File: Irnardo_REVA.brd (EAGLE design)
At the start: 12 x 17 mm, 20 parts, among them J1 USB_PAD, U1 ATMEGA32U4-MU, U2 TSOP755, X1 16MHz

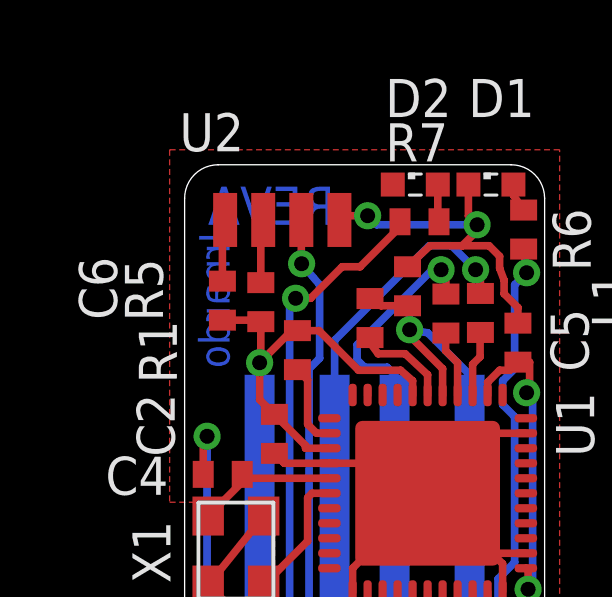
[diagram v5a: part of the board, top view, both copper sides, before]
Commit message: Fix de-couple cap on IR receiver
C6 de-coupling U2 was wrong side of R5.
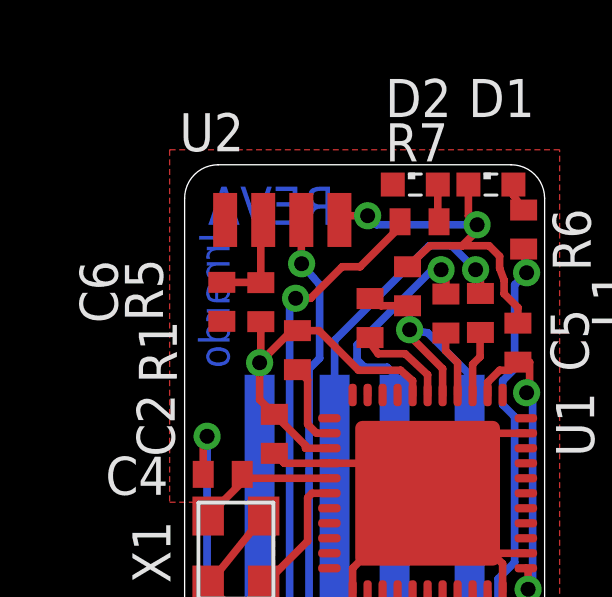
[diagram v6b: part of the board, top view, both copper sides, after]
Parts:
- turned C6 to 270 degrees
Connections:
- net +5V: no longer C6.1
- net N$5: now also C6.1
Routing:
- net GND: track 49.5 -> 47.6 mm
- net N$5: track 2.12 -> 3.43 mm
- net +5V: track 47.7 -> 46.5 mm
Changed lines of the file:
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@@
 <?xml version="1.0" encoding="utf-8"?>
 <!DOCTYPE eagle SYSTEM "eagle.dtd">
-<eagle version="6.4">
+<eagle version="6.5.0">
 <drawing>
 <settings>
@@
 <layers>
 <layer number="1" name="Top" color="4" fill="1" visible="yes" active="yes"/>
-<layer number="16" name="Bottom" color="1" fill="1" visible="no" active="yes"/>
+<layer number="16" name="Bottom" color="1" fill="1" visible="yes" active="yes"/>
 <layer number="17" name="Pads" color="2" fill="1" visible="yes" active="yes"/>
 <layer number="18" name="Vias" color="2" fill="1" visible="yes" active="yes"/>
-<layer number="19" name="Unrouted" color="6" fill="1" visible="no" active="yes"/>
-<layer number="20" name="Dimension" color="15" fill="1" visible="no" active="yes"/>
-<layer number="21" name="tPlace" color="7" fill="1" visible="no" active="yes"/>
-<layer number="22" name="bPlace" color="7" fill="1" visible="no" active="yes"/>
-<layer number="23" name="tOrigins" color="15" fill="1" visible="no" active="yes"/>
-<layer number="24" name="bOrigins" color="15" fill="1" visible="no" active="yes"/>
-<layer number="25" name="tNames" color="7" fill="1" visible="no" active="yes"/>
+<layer number="19" name="Unrouted" color="6" fill="1" visible="yes" active="yes"/>
+<layer number="20" name="Dimension" color="15" fill="1" visible="yes" active="yes"/>
+<layer number="21" name="tPlace" color="7" fill="1" visible="yes" active="yes"/>
+<layer number="22" name="bPlace" color="7" fill="1" visible="yes" active="yes"/>
+<layer number="23" name="tOrigins" color="15" fill="1" visible="yes" active="yes"/>
+<layer number="24" name="bOrigins" color="15" fill="1" visible="yes" active="yes"/>
+<layer number="25" name="tNames" color="7" fill="1" visible="yes" active="yes"/>
 <layer number="26" name="bNames" color="7" fill="1" visible="no" active="yes"/>
 <layer number="27" name="tValues" color="7" fill="1" visible="no" active="yes"/>
@@
 <layer number="37" name="tTest" color="7" fill="1" visible="no" active="yes"/>
 <layer number="38" name="bTest" color="7" fill="1" visible="no" active="yes"/>
-<layer number="39" name="tKeepout" color="4" fill="11" visible="no" active="yes"/>
-<layer number="40" name="bKeepout" color="1" fill="11" visible="no" active="yes"/>
+<layer number="39" name="tKeepout" color="4" fill="11" visible="yes" active="yes"/>
+<layer number="40" name="bKeepout" color="1" fill="11" visible="yes" active="yes"/>
 <layer number="41" name="tRestrict" color="4" fill="10" visible="no" active="yes"/>
 <layer number="42" name="bRestrict" color="1" fill="10" visible="no" active="yes"/>
@@
 <attribute name="NAME" x="-0.17" y="17.45" size="1.27" layer="21"/>
 </element>
-<element name="C6" library="resistor" package="C0402" value="100n" x="1.26" y="12.47" smashed="yes" rot="R90">
-<attribute name="NAME" x="-2.252" y="11.835" size="1.27" layer="25" rot="R90"/>
-<attribute name="VALUE" x="3.165" y="11.835" size="1.27" layer="27" rot="R90"/>
+<element name="C6" library="resistor" package="C0402" value="100n" x="1.24" y="12.43" smashed="yes" rot="R270">
+<attribute name="NAME" x="-3.498" y="13.815" size="1.27" layer="25" rot="R270"/>
+<attribute name="VALUE" x="-0.665" y="13.065" size="1.27" layer="27" rot="R270"/>
 </element>
 <element name="R5" library="resistor" package="R0402" value="100R" x="2.54" y="12.42" smashed="yes" rot="R90">
@@
 <contactref element="C7" pad="1"/>
 <contactref element="R5" pad="1"/>
-<contactref element="C6" pad="1"/>
 <contactref element="J1" pad="V+"/>
 <wire x1="11.11" y1="10.42" x2="10.84" y2="10.15" width="0.254" layer="1"/>
@@
 <wire x1="2.54" y1="11.77" x2="2.54" y2="10.44" width="0.254" layer="1"/>
 <wire x1="2.54" y1="10.44" x2="2.5" y2="10.4" width="0.254" layer="1"/>
-<wire x1="1.26" y1="11.82" x2="2.49" y2="11.82" width="0.254" layer="1"/>
 <wire x1="2.49" y1="11.82" x2="2.54" y2="11.77" width="0.254" layer="1"/>
 <wire x1="4.03" y1="7.55" x2="4.03" y2="7.64" width="0.254" layer="1"/>
@@
 <contactref element="C4" pad="2"/>
 <contactref element="L1" pad="2"/>
-<contactref element="C6" pad="2"/>
 <contactref element="U2" pad="1"/>
 <contactref element="U2" pad="4"/>
@@
 <wire x1="5.6" y1="3.55" x2="8.1" y2="6.05" width="0.254" layer="1"/>
 <wire x1="2.635" y1="5.29" x2="0.785" y2="2.99" width="0.254" layer="1"/>
-<wire x1="1.26" y1="13.12" x2="1.26" y2="15.07" width="0.254" layer="1"/>
 <wire x1="1.26" y1="15.07" x2="1.35" y2="15.16" width="0.254" layer="1"/>
 <wire x1="9.46" y1="16.34" x2="9.46" y2="15.29" width="0.254" layer="1"/>
@@
 <wire x1="9.25" y1="14.3" x2="9.75" y2="14.8" width="0.254" layer="1"/>
 <wire x1="9.75" y1="14.8" x2="9.75" y2="15" width="0.254" layer="1"/>
+<contactref element="C6" pad="2"/>
 </signal>
 <signal name="RESET">
@@
 <wire x1="2.54" y1="13.07" x2="2.54" y2="15.08" width="0.254" layer="1"/>
 <wire x1="2.54" y1="15.08" x2="2.62" y2="15.16" width="0.254" layer="1"/>
+<contactref element="C6" pad="1"/>
+<wire x1="1.24" y1="13.08" x2="2.54" y2="13.08" width="0.254" layer="1"/>
+<wire x1="2.54" y1="13.08" x2="2.54" y2="13.07" width="0.254" layer="1"/>
 </signal>
 <signal name="IO13">

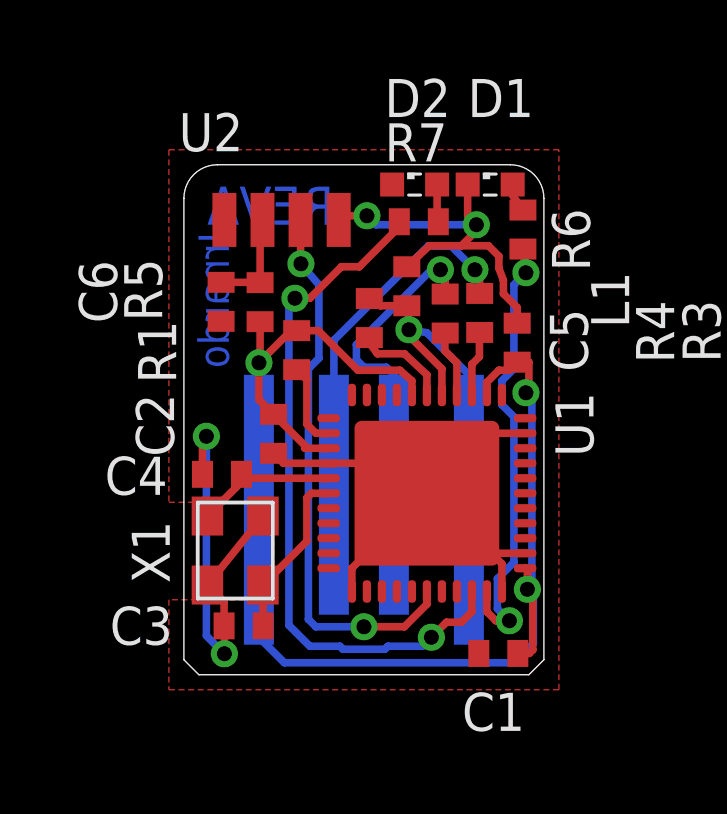
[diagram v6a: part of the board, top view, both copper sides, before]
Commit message: Swap XTAL for 2.5x2mm model
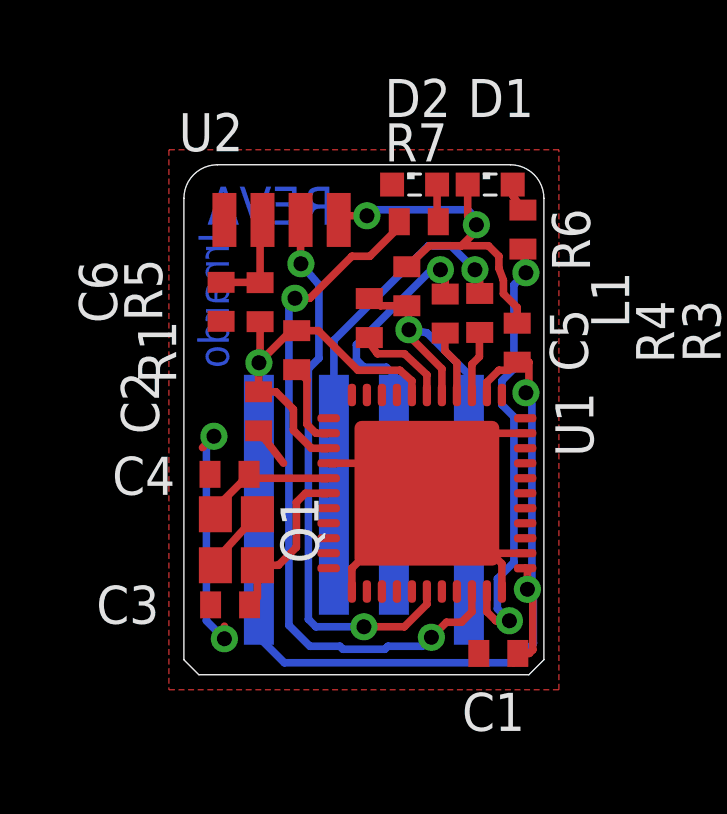
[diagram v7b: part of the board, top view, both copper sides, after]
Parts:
- removed X1: 16MHz, Arduino_Leonardo-REV3b:SMARTPRJ_CRYSTAL-3.2-2.5
- added Q1: FA-20H, crystal:FA-20H
- moved C2 0.90 mm to (2.49, 8.78)
- moved C3 0.83 mm to (1.54, 2.33)
- moved C4 0.25 mm to (1.52, 6.68)
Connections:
- net GND: now also Q1.2, Q1.4; no longer X1.2, X1.4
- net N$1: now also C4.1, Q1.1, U1.16; no longer C3.1, U1.17, X1.1
- net N$2: now also C3.1, Q1.3, U1.17; no longer C4.1, U1.16, X1.3
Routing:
- net GND: track 47.6 -> 43.0 mm
- net N$2: track 4.82 -> 5.94 mm
- net N$1: track 5.67 -> 4.93 mm

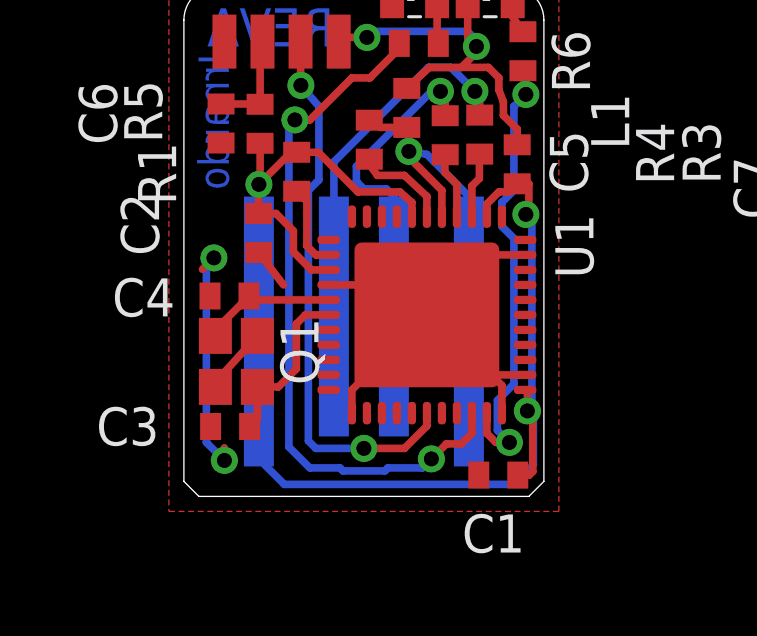
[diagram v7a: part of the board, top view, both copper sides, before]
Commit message: Finish tweaks after move to 2.5mm XTAL
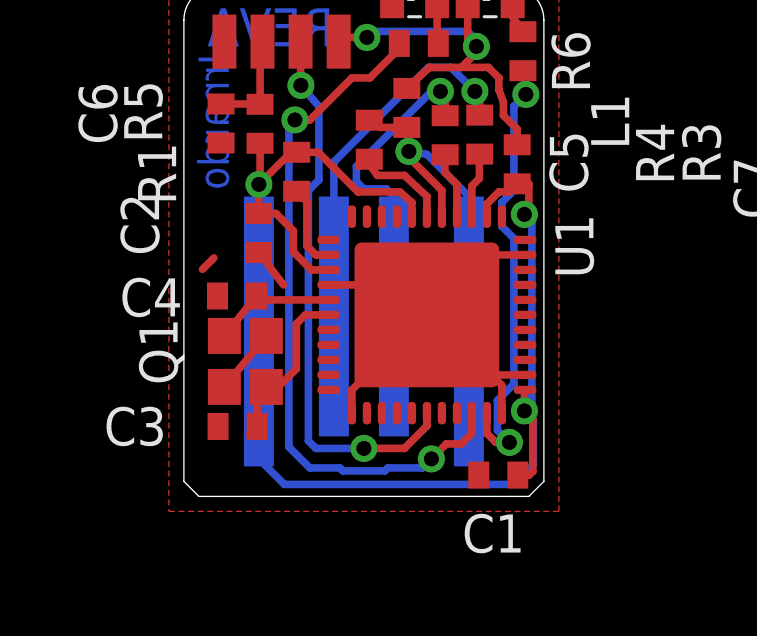
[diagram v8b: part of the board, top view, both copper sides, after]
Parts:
- moved Q1 0.30 mm to (2.05, 4.50)
- moved C3 0.25 mm to (1.79, 2.33)
- moved C4 0.25 mm to (1.77, 6.68)
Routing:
- net GND: track 43.0 -> 35.2 mm, vias 4 -> 2
- net N$1: track 4.93 -> 4.24 mm
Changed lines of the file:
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@@
 <?xml version="1.0" encoding="utf-8"?>
 <!DOCTYPE eagle SYSTEM "eagle.dtd">
-<eagle version="6.5.0">
+<eagle version="6.4">
 <drawing>
 <settings>
@@
 <attribute name="VALUE" x="11.115" y="2.615" size="1.27" layer="27" rot="R180"/>
 </element>
-<element name="C3" library="resistor" package="C0402" value="22p" x="1.54" y="2.33" smashed="yes" rot="R180">
-<attribute name="NAME" x="-0.825" y="2.968" size="1.27" layer="25" rot="R180"/>
-<attribute name="VALUE" x="2.175" y="4.235" size="1.27" layer="27" rot="R180"/>
-</element>
-<element name="C4" library="resistor" package="C0402" value="22p" x="1.52" y="6.68" smashed="yes" rot="R180">
-<attribute name="NAME" x="-0.295" y="7.268" size="1.27" layer="25" rot="R180"/>
-<attribute name="VALUE" x="2.155" y="8.585" size="1.27" layer="27" rot="R180"/>
+<element name="C3" library="resistor" package="C0402" value="22p" x="1.79" y="2.33" smashed="yes" rot="R180">
+<attribute name="NAME" x="-0.575" y="2.968" size="1.27" layer="25" rot="R180"/>
+<attribute name="VALUE" x="2.425" y="4.235" size="1.27" layer="27" rot="R180"/>
+</element>
+<element name="C4" library="resistor" package="C0402" value="22p" x="1.77" y="6.68" smashed="yes" rot="R180">
+<attribute name="NAME" x="-0.045" y="7.268" size="1.27" layer="25" rot="R180"/>
+<attribute name="VALUE" x="2.405" y="8.585" size="1.27" layer="27" rot="R180"/>
 </element>
 <element name="C2" library="resistor" package="C0402" value="100n" x="2.49" y="8.78" smashed="yes" rot="R270">
@@
 <attribute name="NAME" x="6.75" y="-1.75" size="1.27" layer="26" rot="MR0"/>
 </element>
-<element name="Q1" library="crystal" package="FA-20H" value="FA-20H" x="1.75" y="4.5" rot="R270"/>
+<element name="Q1" library="crystal" package="FA-20H" value="FA-20H" x="2.05" y="4.5" smashed="yes" rot="R270">
+<attribute name="NAME" x="-1.48" y="5.945" size="1.27" layer="25" rot="R270"/>
+<attribute name="VALUE" x="-0.7" y="5.95" size="1.27" layer="27" rot="R270"/>
+</element>
 </elements>
 <signals>
@@
 <wire x1="2.5" y1="10.4" x2="2.5" y2="10.5" width="0.254" layer="16"/>
 <wire x1="2.5" y1="10.4" x2="2.5" y2="5.5" width="0.254" layer="16"/>
-<wire x1="11.38" y1="3.545" x2="11.375" y2="3.55" width="0.254" layer="1"/>
 <wire x1="3.76" y1="11.47" x2="3.57" y2="11.47" width="0.254" layer="1"/>
 <wire x1="3.57" y1="11.47" x2="2.5" y2="10.4" width="0.254" layer="1"/>
@@
 <wire x1="11.13" y1="0.71" x2="11.51" y2="0.71" width="0.254" layer="1"/>
 <wire x1="11.51" y1="0.71" x2="11.63" y2="0.83" width="0.254" layer="1"/>
-<wire x1="11.63" y1="0.83" x2="11.63" y2="2.67" width="0.254" layer="1"/>
-<wire x1="11.63" y1="2.67" x2="11.45" y2="2.85" width="0.254" layer="1"/>
-<via x="11.45" y="2.85" extent="1-16" drill="0.5"/>
-<wire x1="11.45" y1="2.85" x2="11.6" y2="3" width="0.254" layer="16"/>
-<wire x1="11.6" y1="3" x2="11.6" y2="9.2" width="0.254" layer="16"/>
-<wire x1="11.6" y1="9.2" x2="11.4" y2="9.4" width="0.254" layer="16"/>
-<via x="11.4" y="9.4" extent="1-16" drill="0.5"/>
-<wire x1="11.4" y1="9.4" x2="11.5" y2="9.5" width="0.254" layer="1"/>
-<wire x1="11.5" y1="9.5" x2="11.5" y2="10.42" width="0.254" layer="1"/>
+<wire x1="11.63" y1="0.83" x2="11.63" y2="2.57" width="0.254" layer="1"/>
+<wire x1="11.63" y1="2.57" x2="11.35" y2="2.85" width="0.254" layer="1"/>
+<via x="11.35" y="2.85" extent="1-16" drill="0.5"/>
+<wire x1="11.35" y1="2.85" x2="11.6" y2="3.1" width="0.254" layer="16"/>
+<wire x1="11.6" y1="3.1" x2="11.6" y2="9.15" width="0.254" layer="16"/>
+<wire x1="11.6" y1="9.15" x2="11.35" y2="9.4" width="0.254" layer="16"/>
+<via x="11.35" y="9.4" extent="1-16" drill="0.5"/>
+<wire x1="11.35" y1="9.4" x2="11.5" y2="9.55" width="0.254" layer="1"/>
+<wire x1="11.5" y1="9.55" x2="11.5" y2="10.42" width="0.254" layer="1"/>
 <wire x1="11.5" y1="10.42" x2="11.11" y2="10.42" width="0.254" layer="1"/>
-<wire x1="11.375" y1="3.55" x2="11.45" y2="3.475" width="0.254" layer="1" curve="-90"/>
-<wire x1="11.45" y1="3.475" x2="11.45" y2="2.85" width="0.254" layer="1"/>
 <wire x1="2.5" y1="5.5" x2="2.5" y2="1.25" width="0.254" layer="16"/>
 <wire x1="2.5" y1="1.25" x2="3.35" y2="0.4" width="0.254" layer="16"/>
 <wire x1="3.35" y1="0.4" x2="11" y2="0.4" width="0.254" layer="16"/>
 <wire x1="11" y1="0.4" x2="11.65" y2="1.05" width="0.254" layer="16"/>
-<wire x1="11.65" y1="1.05" x2="11.65" y2="2.6" width="0.254" layer="16"/>
-<wire x1="11.65" y1="2.6" x2="11.5" y2="2.75" width="0.254" layer="16"/>
+<wire x1="11.65" y1="1.05" x2="11.65" y2="2.55" width="0.254" layer="16"/>
 <wire x1="7.6" y1="9.325" x2="7.6" y2="9.8" width="0.254" layer="1"/>
 <wire x1="7.6" y1="9.8" x2="7.2" y2="10.15" width="0.254" layer="1"/>
@@
 <wire x1="3.65" y1="8.85" x2="3.07" y2="9.43" width="0.254" layer="1"/>
 <wire x1="3.07" y1="9.43" x2="2.49" y2="9.43" width="0.254" layer="1"/>
-<wire x1="11.65" y1="2.6" x2="11.63" y2="2.67" width="0" layer="19" extent="1-16"/>
+<wire x1="11.65" y1="2.55" x2="11.35" y2="2.85" width="0.254" layer="16"/>
+<wire x1="11.375" y1="3.55" x2="11.35" y2="3.525" width="0.254" layer="1"/>
+<wire x1="11.35" y1="3.525" x2="11.35" y2="2.85" width="0.254" layer="1"/>
 </signal>
 <signal name="GND">
@@
 <wire x1="5.3" y1="15.3" x2="5.16" y2="15.16" width="0.254" layer="1"/>
 <wire x1="0.62" y1="7.57" x2="1" y2="7.95" width="0.254" layer="1"/>
-<via x="1" y="7.95" extent="1-16" drill="0.5"/>
-<wire x1="0.75" y1="1.8" x2="1.35" y2="1.2" width="0.254" layer="16"/>
-<via x="1.35" y="1.2" extent="1-16" drill="0.5"/>
-<wire x1="1.35" y1="1.2" x2="1.35" y2="1.62" width="0.254" layer="1"/>
 <wire x1="7.43" y1="13.6" x2="8.18" y2="14.3" width="0.254" layer="1"/>
 <wire x1="8.18" y1="14.3" x2="9.25" y2="14.3" width="0.254" layer="1"/>
@@
 <wire x1="3.32" y1="7.05" x2="2.49" y2="8.13" width="0.254" layer="1"/>
 <wire x1="11.375" y1="8.05" x2="10.1" y2="8.05" width="0.254" layer="1"/>
-<wire x1="2.45" y1="5.35" x2="1" y2="3.75" width="0.254" layer="1"/>
-<wire x1="1" y1="8" x2="0.75" y2="8" width="0.254" layer="16"/>
-<wire x1="0.75" y1="8" x2="0.75" y2="1.8" width="0.254" layer="16"/>
-<wire x1="1.05" y1="3.65" x2="1" y2="3.7" width="0.254" layer="1"/>
-<wire x1="1" y1="3.7" x2="1" y2="3.75" width="0.254" layer="1"/>
 <wire x1="6.1" y1="15.3" x2="6.3" y2="15.5" width="0.254" layer="16"/>
 <wire x1="6.3" y1="15.5" x2="9.46" y2="15.5" width="0.254" layer="16"/>
 <wire x1="9.46" y1="15.5" x2="9.75" y2="15.21" width="0.254" layer="16"/>
 <wire x1="9.75" y1="15.21" x2="9.75" y2="15" width="0.254" layer="16"/>
+<wire x1="2.75" y1="5.35" x2="1.35" y2="3.65" width="0.254" layer="1"/>
 </signal>
 <signal name="RESET">
@@
 <contactref element="Q1" pad="1"/>
 <contactref element="C4" pad="1"/>
-<wire x1="1.05" y1="5.35" x2="0.8" y2="5.3" width="0.254" layer="1"/>
-<wire x1="1.92" y1="6.42" x2="2.17" y2="6.68" width="0.254" layer="1"/>
-<wire x1="2.05" y1="6.55" x2="2.17" y2="6.68" width="0.254" layer="1" curve="-90"/>
-<wire x1="4.825" y1="6.55" x2="2.3" y2="6.55" width="0.254" layer="1"/>
-<wire x1="2.3" y1="6.55" x2="2.17" y2="6.68" width="0.254" layer="1" curve="-90"/>
-<wire x1="1.92" y1="6.42" x2="1.05" y2="5.55" width="0.254" layer="1"/>
-<wire x1="1.05" y1="5.55" x2="1.05" y2="5.35" width="0.254" layer="1"/>
+<wire x1="4.825" y1="6.55" x2="2.42" y2="6.55" width="0.254" layer="1"/>
+<wire x1="2.42" y1="6.55" x2="2.42" y2="6.68" width="0.254" layer="1"/>
+<wire x1="2.42" y1="6.68" x2="1.35" y2="5.35" width="0.254" layer="1"/>
 </signal>
 <signal name="N$2">
@@
 <contactref element="Q1" pad="3"/>
 <contactref element="U1" pad="17"/>
-<wire x1="2.19" y1="2.33" x2="2.2" y2="2.07" width="0.254" layer="1"/>
-<wire x1="2.19" y1="2.33" x2="2.45" y2="2.59" width="0.254" layer="1"/>
-<wire x1="2.45" y1="2.59" x2="2.45" y2="3.65" width="0.254" layer="1"/>
-<wire x1="2.45" y1="3.65" x2="3.15" y2="3.65" width="0.254" layer="1"/>
-<wire x1="3.15" y1="3.65" x2="3.75" y2="4.25" width="0.254" layer="1"/>
+<wire x1="2.44" y1="2.33" x2="2.2" y2="2.07" width="0.254" layer="1"/>
+<wire x1="2.44" y1="2.33" x2="2.45" y2="2.59" width="0.254" layer="1"/>
 <wire x1="3.75" y1="4.25" x2="3.75" y2="5.75" width="0.254" layer="1"/>
 <wire x1="3.75" y1="5.75" x2="4.05" y2="6.05" width="0.254" layer="1"/>
 <wire x1="4.05" y1="6.05" x2="4.825" y2="6.05" width="0.254" layer="1"/>
+<wire x1="3.75" y1="4.25" x2="3.15" y2="3.65" width="0.254" layer="1"/>
+<wire x1="3.15" y1="3.65" x2="2.75" y2="3.65" width="0.254" layer="1"/>
+<wire x1="2.75" y1="3.65" x2="2.44" y2="3.34" width="0.254" layer="1"/>
+<wire x1="2.44" y1="3.34" x2="2.44" y2="2.33" width="0.254" layer="1"/>
 </signal>
 </signals>
